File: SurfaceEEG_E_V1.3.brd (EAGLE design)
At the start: 30 x 26 mm, 10 parts, among them IC1 LMP7702

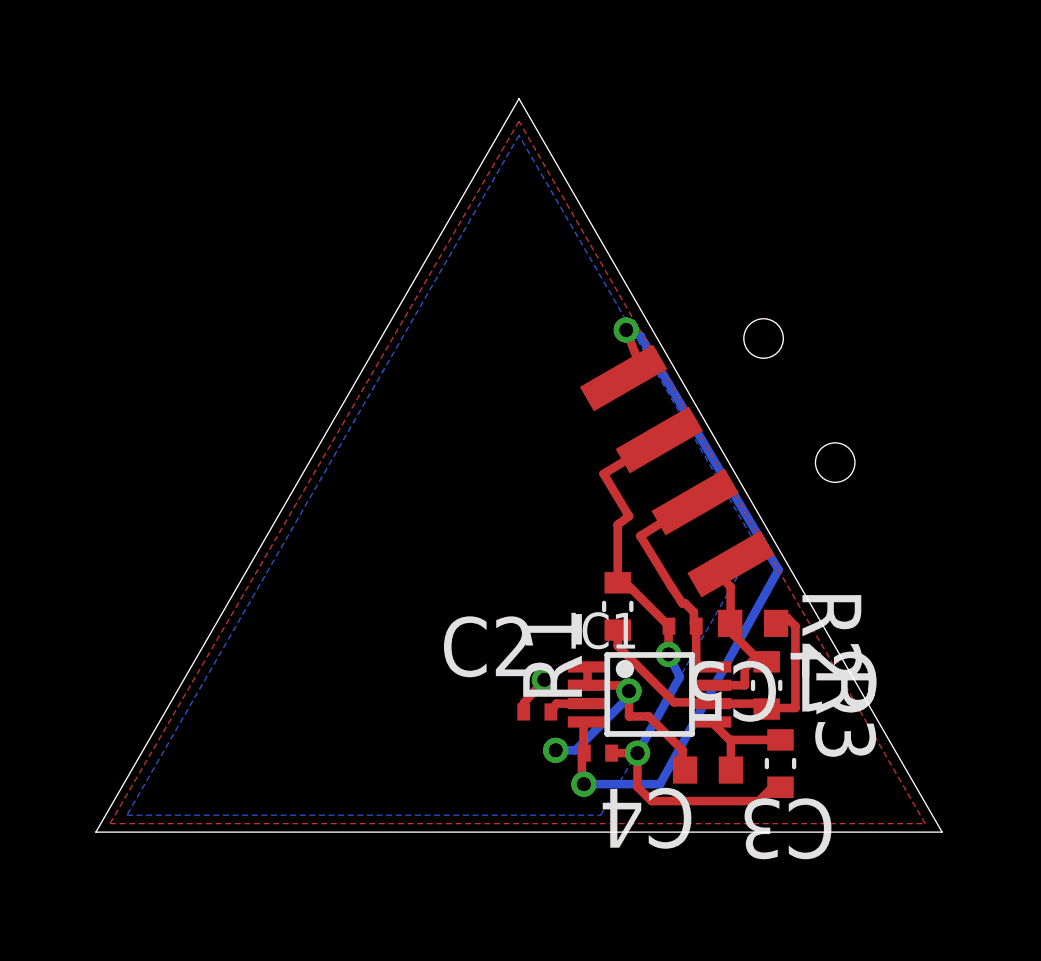
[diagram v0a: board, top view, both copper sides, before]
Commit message: Updated SurfaceEEG_E
Updated SurfaceEEG_E to V1.3. Replaced solder pads. Improved layout and
checked DRC.
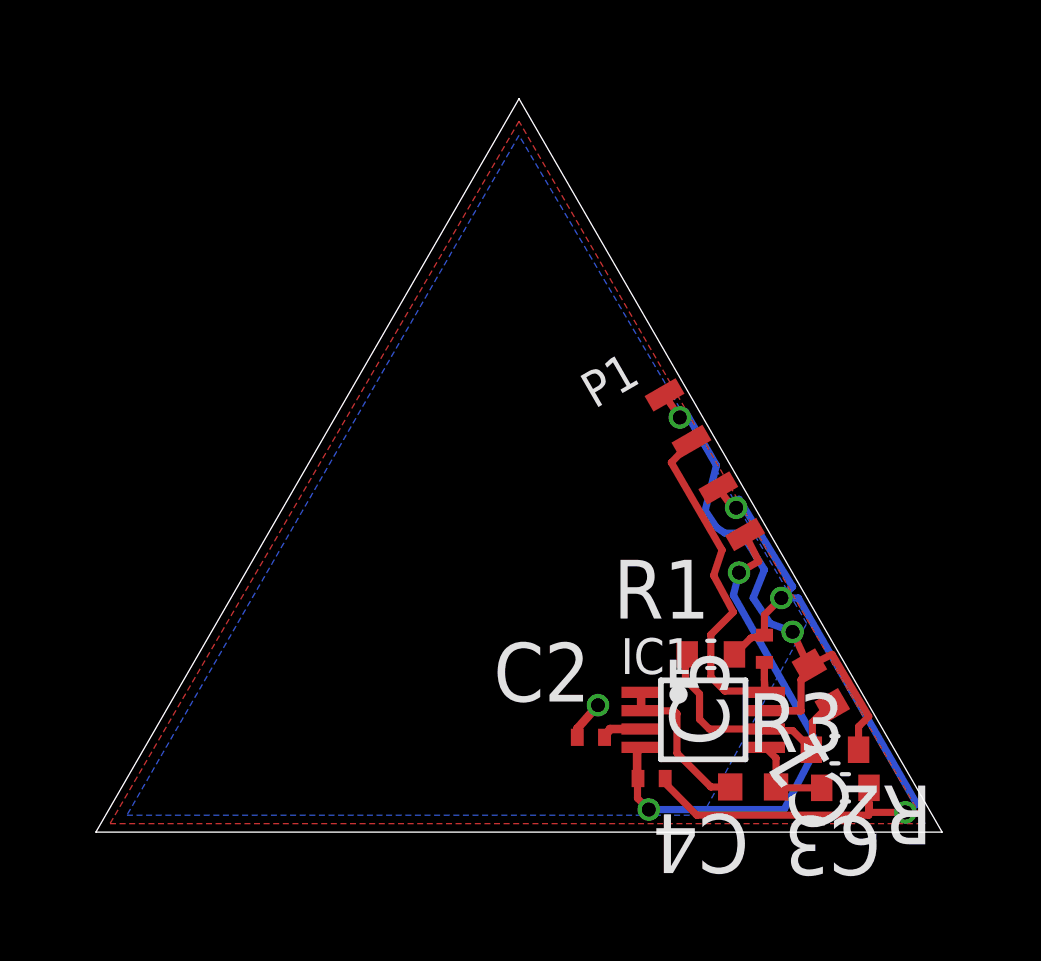
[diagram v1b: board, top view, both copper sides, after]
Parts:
- P1: value (none) -> SOLDERPAD4-1.27-2.54; device SparkFun-Connectors:1X04-SMD -> (custom)-new-components:SMD1,27-2,54
- moved P1 4.78 mm to (20.2, 15.5), turned to 300 degrees
- moved R1 3.71 mm to (21.8, 6.30), turned to 0 degrees
- moved R2 3.32 mm to (26.2, 2.92), turned to 180 degrees
- moved C1 3.26 mm to (25.7, 5.20), turned to 120 degrees
- moved C5 3.01 mm to (23.7, 6.50), turned to 90 degrees
- moved R3 2.46 mm to (26.6, 1.57), turned to 0 degrees
- moved IC1 2.10 mm to (21.5, 3.98)
- moved C2 2.10 mm to (17.6, 3.36)
- moved C4 2.10 mm to (19.7, 1.90)
- moved C3 1.71 mm to (23.3, 1.60)
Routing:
- net N$4: track 7.44 -> 22.3 mm, vias 0 -> 2
- net AGND: track 21.8 -> 28.4 mm, vias 2 -> 3
- net GND: track 26.1 -> 19.9 mm
- net +3V3: track 8.38 -> 13.9 mm
- net SHIELD: track 9.48 -> 5.75 mm, vias 2 -> 0
- net N$2: track 11.8 -> 9.02 mm
- net N$3: track 3.76 -> 3.19 mm

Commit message: Updated all boards in order to comply with DRC
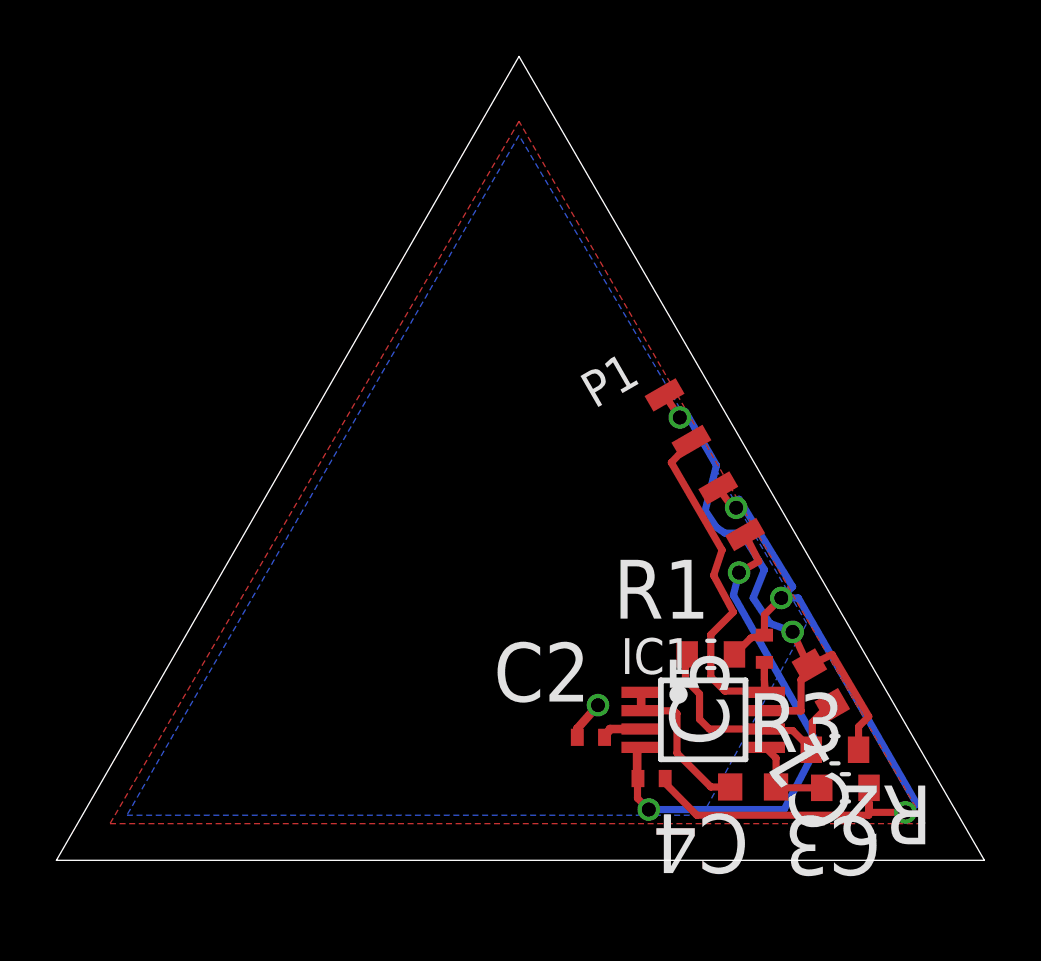
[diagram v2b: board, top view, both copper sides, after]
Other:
- board size 30 x 26 mm -> 32.9 x 28.5 mm
